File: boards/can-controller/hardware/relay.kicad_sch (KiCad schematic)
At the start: 26 parts, among them J30 RELAY, U30 ISO6740, U31 ISO6740, U32 ULN2803A

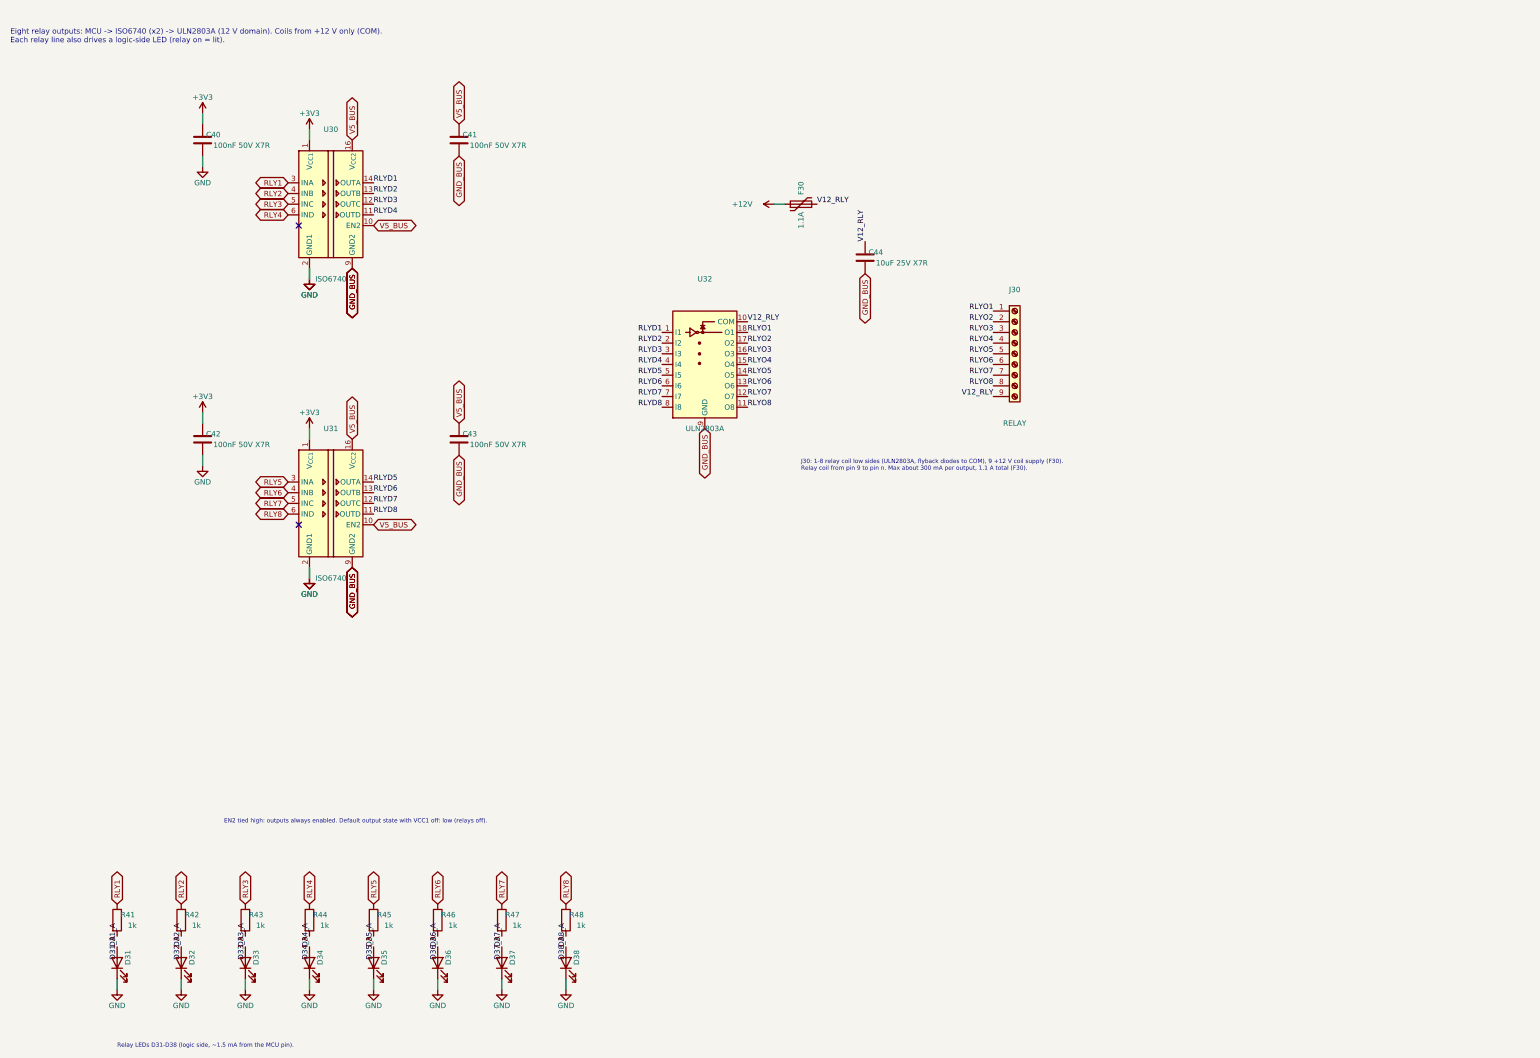
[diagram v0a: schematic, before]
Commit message: can-controller: double-level push-in terminals, re-placement, no DIN clips
- Phoenix SPTD 1,5 footprints (3-8 positions) generated from the Phoenix
  drawing (lib/footprint_src/Thl_Connector/phoenix_sptd.py)
- Schematic: J40 GPIO 2x8 (GPIO1-8 / GND), J50 ANALOG 2x6 (AI1-4, AO1-2 /
  GND), J30 RELAY 2x8 (OUT1-8 / +12 V); relay LEDs moved to the 12 V side
  (+12 V -> 4.7k -> LED -> OUTn); J41 removed
- Placement rev 2: GPIO and analog on the left edge, relay on the bottom;
  12 V block x > 140, y > 160 plus the CAN strip; all ISO1044 on x = 168;
  relay LEDs behind their terminal pins; CAN LEDs in a column
- DIN clip holes removed (3D-printed adapter on the M2.5 holes instead)
- DRC clean apart from unrouted nets and silkscreen

Co-Authored-By: Claude Opus 5.5 <noreply@anthropic.com>
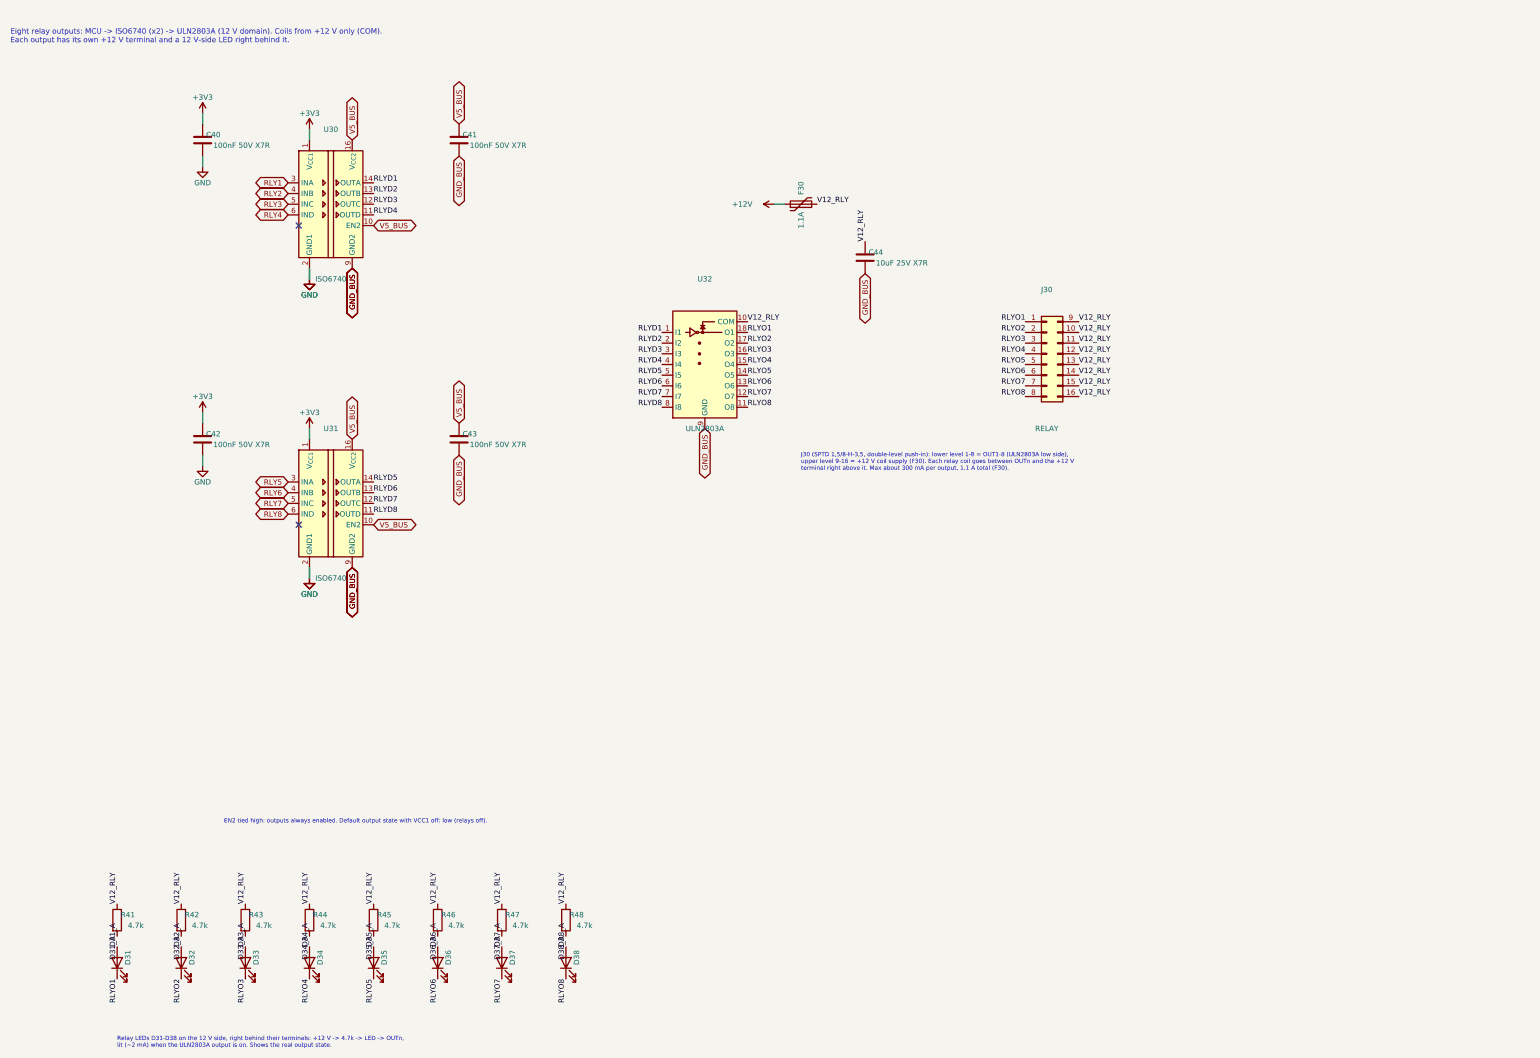
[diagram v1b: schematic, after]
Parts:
- removed J30: RELAY, Connector_Phoenix_MC:PhoenixContact_MC_1,5_9-G-3.5_1x09_P3.50mm_Horizontal, symbol Connector:Screw_Terminal_01x09
- added J30: RELAY, Thl_Connector:PhoenixContact_SPTD_1,5_8-H-3,5_2x08_P3.5mm_Horizontal, symbol Connector_Generic:Conn_02x08_Top_Bottom
- R41, R42, R43, R44, R45, R46, R47, R48: value 1k -> 4.7k; MPN RC1206FR-071KL -> RC1206FR-074K7L
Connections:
- net GND: no longer D31.1 (K), D32.1 (K), D33.1 (K), D34.1 (K), D35.1 (K), D36.1 (K), D37.1 (K), D38.1 (K)
- net RLY1: no longer R41.1
- net RLY2: no longer R42.1
- net RLY3: no longer R43.1
- net RLY4: no longer R44.1
- net RLY5: no longer R45.1
- net RLY6: no longer R46.1
- net RLY7: no longer R47.1
- net RLY8: no longer R48.1
- net RLYO1: now also D31.1 (K), J30.1 (Pin_1)
- net RLYO2: now also D32.1 (K), J30.2 (Pin_2)
- net RLYO3: now also D33.1 (K), J30.3 (Pin_3)
- net RLYO4: now also D34.1 (K), J30.4 (Pin_4)
- net RLYO5: now also D35.1 (K), J30.5 (Pin_5)
- net RLYO6: now also D36.1 (K), J30.6 (Pin_6)
- net RLYO7: now also D37.1 (K), J30.7 (Pin_7)
- net RLYO8: now also D38.1 (K), J30.8 (Pin_8)
- net V12_RLY: now also R41.1, R42.1, R43.1, R44.1, R45.1, R46.1, R47.1, R48.1, J30.10 (Pin_10), J30.11 (Pin_11), J30.12 (Pin_12), J30.13 (Pin_13), J30.14 (Pin_14), J30.15 (Pin_15), J30.16 (Pin_16), J30.9 (Pin_9)
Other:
- note added: "Eight relay outputs: MCU -> ISO6740 (x2) -> ULN2803A (12 V domain). Coils from +12 V only (COM). Each output has its own +12 V terminal and a 12 V-side LED right behind it."
- note added: "J30 (SPTD 1,5/8-H-3,5, double-level push-in): lower level 1-8 = OUT1-8 (ULN2803A low side), upper level 9-16 = +12 V coil supply (F30). Each relay coil goes between OUTn and the +12 V terminal right above it. Max about 300 mA per output, 1.1 A total (F30)."
- note added: "Relay LEDs D31-D38 on the 12 V side, right behind their terminals: +12 V -> 4.7k -> LED -> OUTn, lit (~2 mA) when the ULN2803A output is on. Shows the real output state."
- note removed: "Eight relay outputs: MCU -> ISO6740 (x2) -> ULN2803A (12 V domain). Coils from +12 V only (COM). Each relay line also drives a logic-side LED (relay on = lit)."
- note removed: "J30: 1-8 relay coil low sides (ULN2803A, flyback diodes to COM), 9 +12 V coil supply (F30). Relay coil from pin 9 to pin n. Max about 300 mA per output, 1.1 A total (F30)."
- note removed: "Relay LEDs D31-D38 (logic side, ~1.5 mA from the MCU pin)."

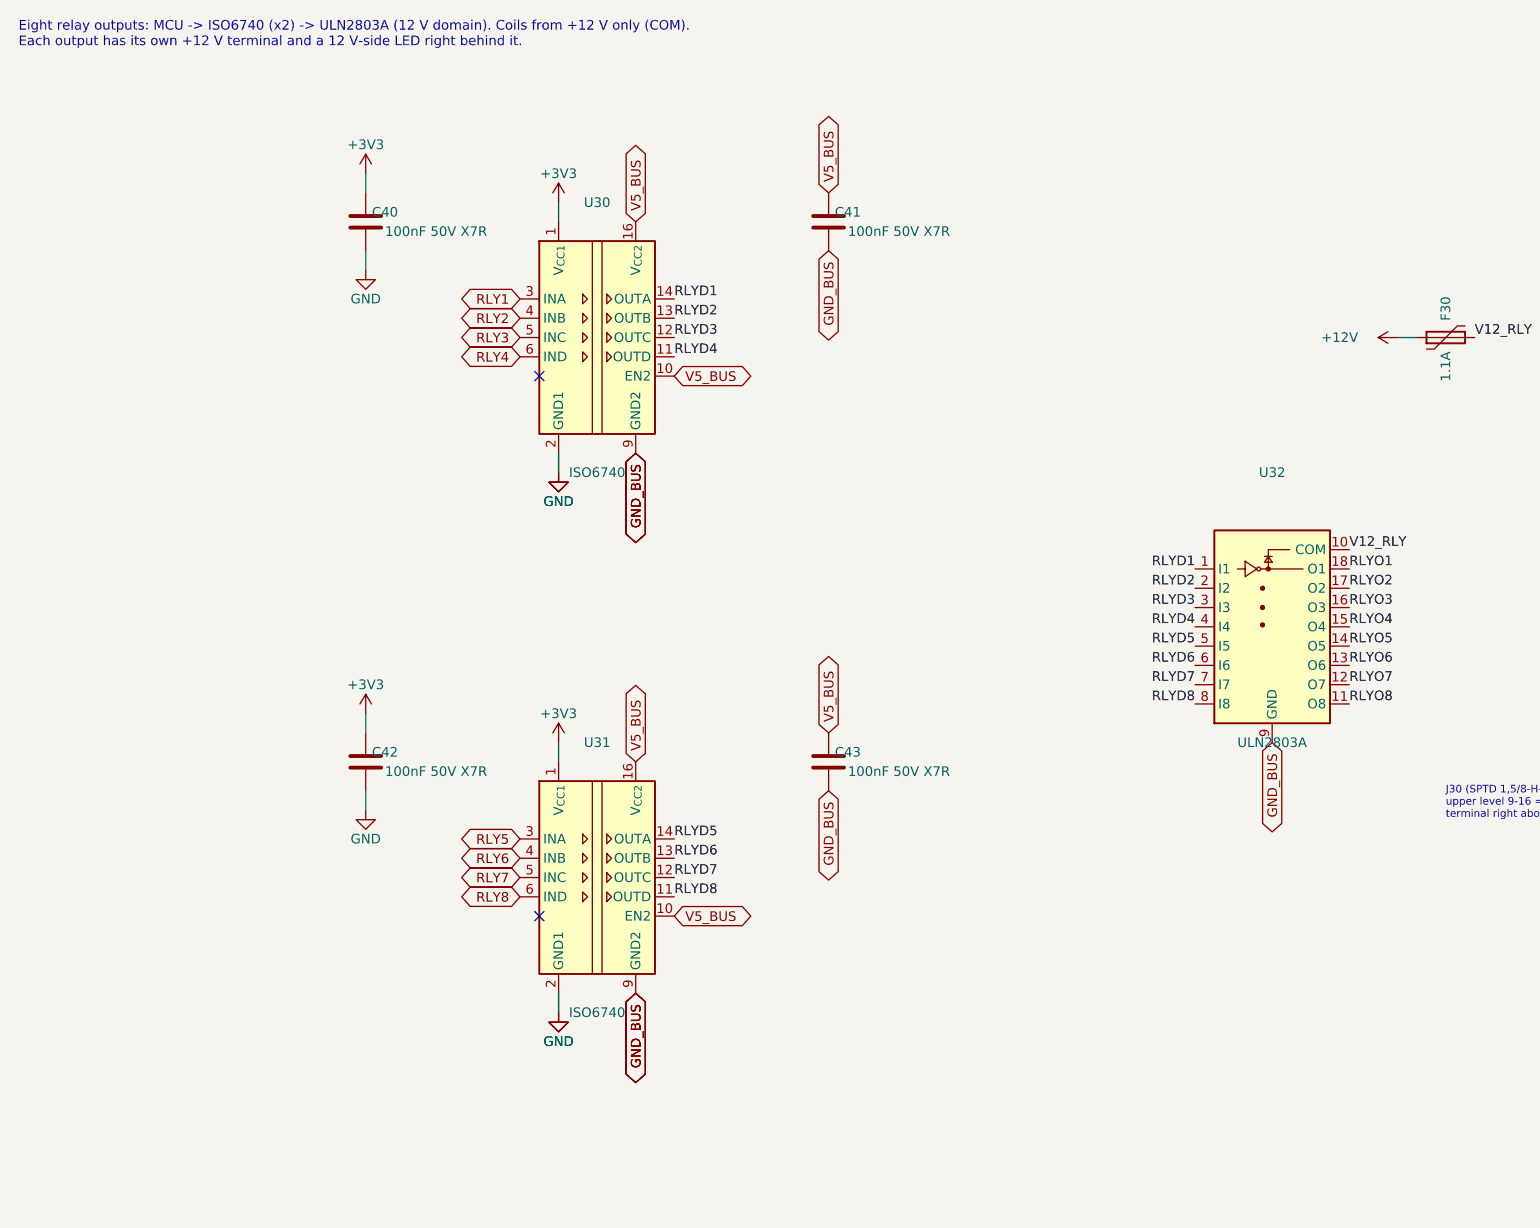
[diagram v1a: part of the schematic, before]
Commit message: can-controller: placement rev 3 so the MCU can fan out, routing WIP
Schematic:
- U1 pin map redone for the MCU rotated 90 deg: each side carries the
  signals for the parts it faces, in order (GPIO left, CAN right, USB /
  crystal / ICSP / UART top, DAC SPI4 / I2C1 bottom). ICSP on PGx2
  (pins 43/44, ICESEL = PGx2), UART1 on 46/47, V12_OK on pin 33.
- Relays driven over I2C1 by an MCP23008 (U33, 0x20); relay channel
  order permuted so expander -> ISO6740 -> ULN2803A -> J30 runs straight
- FB1 removed, AVDD tied to +3V3 (sits between two CAN pin pairs)
- J50 pinout: 1-2 AO1/AO2, 3-6 AI1-4 (outputs no longer cross inputs)
- Interface_Expansion:MCP23008-xSO imported to lib/

PCB:
- place_rev3.py: U1 rotated at (148,131), expander under it, relay
  isolators across the 12 V block's top edge (corner now x = 134),
  ULN below, 12 V opto at the top of the CAN strip, analog section
  re-laid around the new J50 pinout; bottom zones follow the new corner
- Routed: MCU escape nets first, signals top only, then power; 8
  connections open, ~48 clearance near-misses to clean up by hand,
  ~370 mm bottom traces

Co-Authored-By: Claude Opus 5.5 <noreply@anthropic.com>
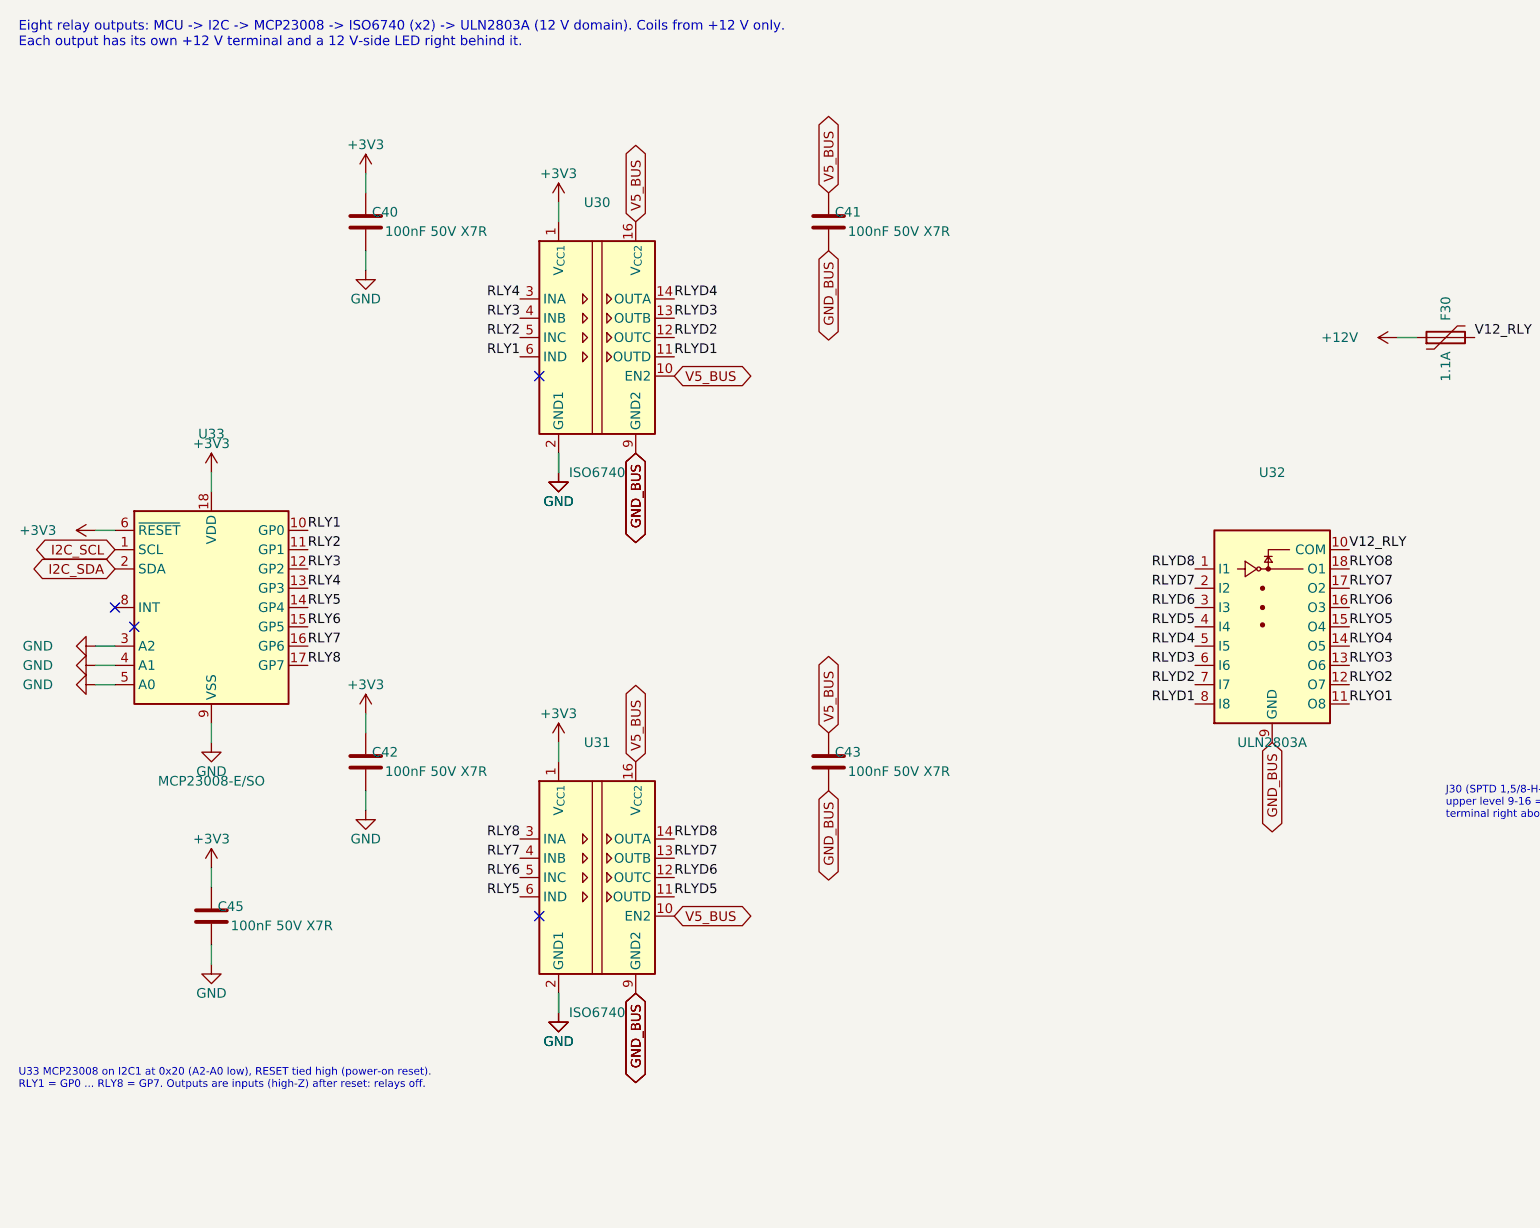
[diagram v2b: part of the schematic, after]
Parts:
- added C45: 100nF 50V X7R, Capacitor_SMD:C_0805_2012Metric_Pad1.18x1.45mm_HandSolder, symbol Device:C
- added U33: MCP23008-E/SO, Package_SO:SOIC-18W_7.5x11.6mm_P1.27mm, symbol Interface_Expansion:MCP23008-xSO
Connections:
- net +3V3: now also C45.1, U33.18 (VDD), U33.6 (~{RESET})
- net GND: now also C45.2, U33.3 (A2), U33.4 (A1), U33.5 (A0), U33.9 (VSS)
- net RLY1: now also U30.6 (IND), U33.10 (GP0); no longer U30.3 (INA)
- net RLY2: now also U30.5 (INC), U33.11 (GP1); no longer U30.4 (INB)
- net RLY3: now also U30.4 (INB), U33.12 (GP2); no longer U30.5 (INC)
- net RLY4: now also U30.3 (INA), U33.13 (GP3); no longer U30.6 (IND)
- net RLY5: now also U31.6 (IND), U33.14 (GP4); no longer U31.3 (INA)
- net RLY6: now also U31.5 (INC), U33.15 (GP5); no longer U31.4 (INB)
- net RLY7: now also U31.4 (INB), U33.16 (GP6); no longer U31.5 (INC)
- net RLY8: now also U31.3 (INA), U33.17 (GP7); no longer U31.6 (IND)
- net RLYD1: now also U30.11 (OUTD), U32.8 (I8); no longer U30.14 (OUTA), U32.1 (I1)
- net RLYD2: now also U30.12 (OUTC), U32.7 (I7); no longer U30.13 (OUTB), U32.2 (I2)
- net RLYD3: now also U30.13 (OUTB), U32.6 (I6); no longer U30.12 (OUTC), U32.3 (I3)
- net RLYD4: now also U30.14 (OUTA), U32.5 (I5); no longer U30.11 (OUTD), U32.4 (I4)
- net RLYD5: now also U31.11 (OUTD), U32.4 (I4); no longer U31.14 (OUTA), U32.5 (I5)
- net RLYD6: now also U31.12 (OUTC), U32.3 (I3); no longer U31.13 (OUTB), U32.6 (I6)
- net RLYD7: now also U31.13 (OUTB), U32.2 (I2); no longer U31.12 (OUTC), U32.7 (I7)
- net RLYD8: now also U31.14 (OUTA), U32.1 (I1); no longer U31.11 (OUTD), U32.8 (I8)
- net RLYO1: now also U32.11 (O8); no longer U32.18 (O1)
- net RLYO2: now also U32.12 (O7); no longer U32.17 (O2)
- net RLYO3: now also U32.13 (O6); no longer U32.16 (O3)
- net RLYO4: now also U32.14 (O5); no longer U32.15 (O4)
- net RLYO5: now also U32.15 (O4); no longer U32.14 (O5)
- net RLYO6: now also U32.16 (O3); no longer U32.13 (O6)
- net RLYO7: now also U32.17 (O2); no longer U32.12 (O7)
- net RLYO8: now also U32.18 (O1); no longer U32.11 (O8)
- new net I2C_SCL: U33.1 (SCL)
- new net I2C_SDA: U33.2 (SDA)
- no-connect marks 2 -> 4
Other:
- note added: "Eight relay outputs: MCU -> I2C -> MCP23008 -> ISO6740 (x2) -> ULN2803A (12 V domain). Coils from +12 V only. Each output has its own +12 V terminal and a 12 V-side LED right behind it."
- note added: "U33 MCP23008 on I2C1 at 0x20 (A2-A0 low), RESET tied high (power-on reset). RLY1 = GP0 ... RLY8 = GP7. Outputs are inputs (high-Z) after reset: relays off."
- note removed: "Eight relay outputs: MCU -> ISO6740 (x2) -> ULN2803A (12 V domain). Coils from +12 V only (COM). Each output has its own +12 V terminal and a 12 V-side LED right behind it."
